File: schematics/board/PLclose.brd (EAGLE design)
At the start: 82 x 82 mm, 38 parts

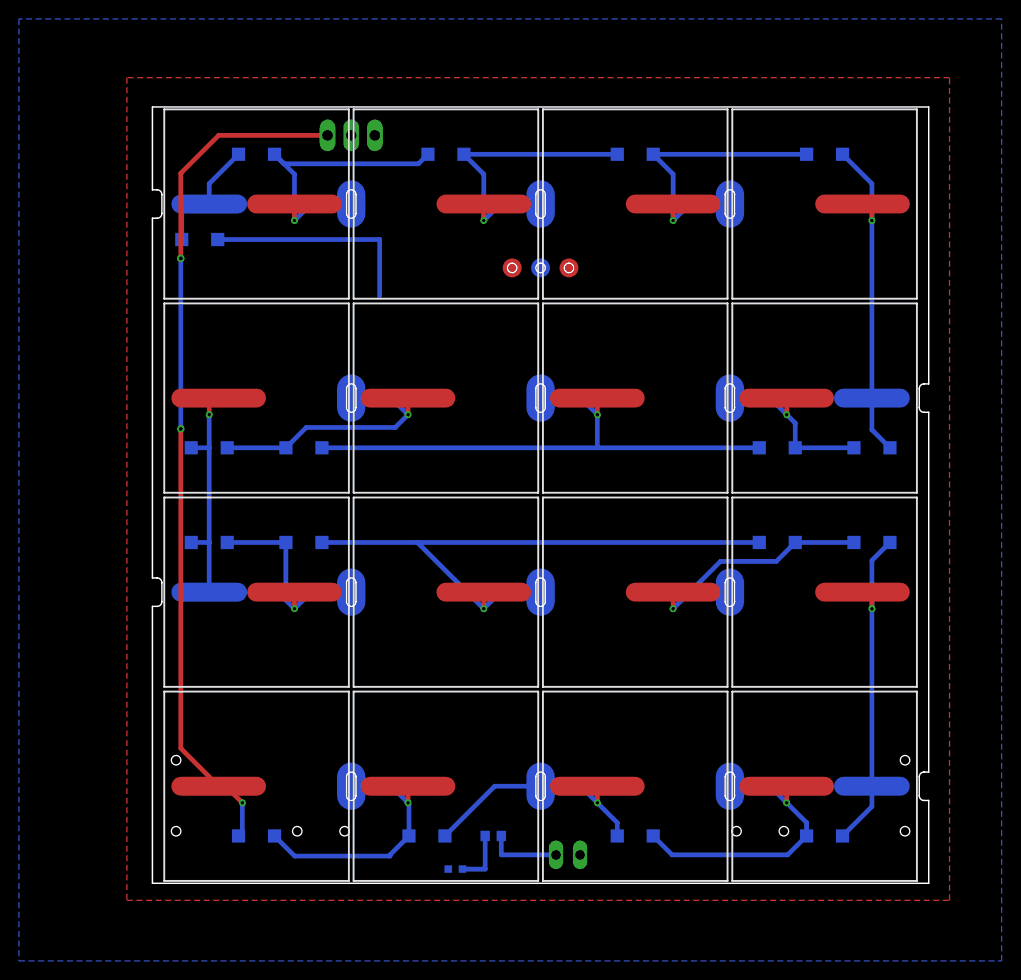
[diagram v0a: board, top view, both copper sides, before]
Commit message: Добавлена схема дозиметра, исправлены платы СБ
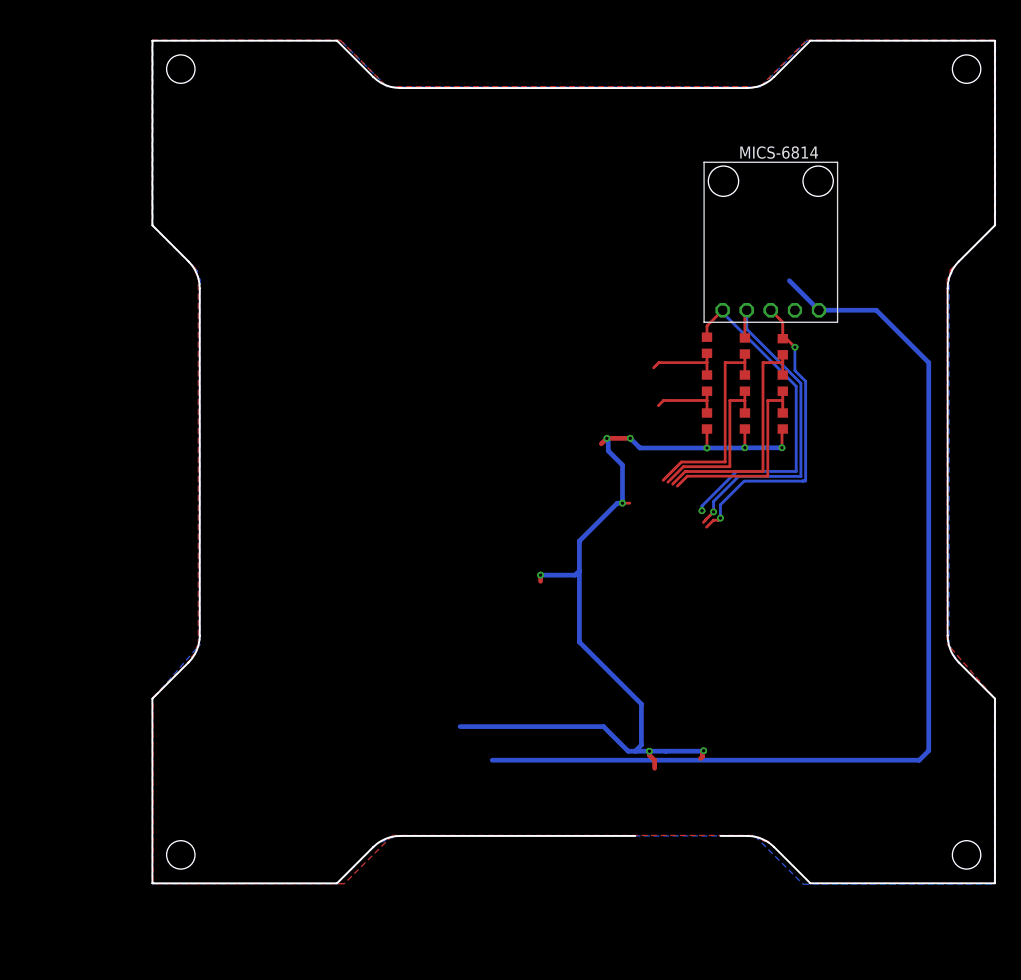
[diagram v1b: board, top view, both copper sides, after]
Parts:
- removed D1, D10, D11, D12, D13, D14, D15, D16, D17, D2, D3, D4, D5, D6, D7, D8, D9: MBR0520LT, diode:SOD123
- removed JP1: (no value), pinhead:1X02
- removed PWR: (no value), led:CHIPLED_0603
- removed R1_2K7: 2k7, rcl:R0603
- removed S1: (no value), CanCubeSat:255SB
- removed SOL1, SOL10, SOL11, SOL13, SOL14, SOL15, SOL2, SOL3, SOL5, SOL6, SOL7, SOL9: SOLAR_0, CanCubeSat:SOLAR_0
- removed SOL12, SOL16, SOL4, SOL8: SOLAR_1, CanCubeSat:SOLAR_1
- removed U$6: GRAFITGRAFIT3_1, CanCubeSat:GRAFIT3_1
- added MICS-6814: MICS-6814, CanCubeSat:MICS-6814
- added R1, R2, R3, R4, R5, R6, R7, R8, R9: 10k, resistor:R0603
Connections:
- removed net BUS+: JP1.2, R1_2K7.1, S1.2
- removed net BUS-: D1.C, JP1.1, PWR.C
- removed net N$1: D16.A, D17.C, SOL1.OUT, SOL2.IN
- removed net N$10: D10.A, D11.C, SOL7.OUT, SOL8.IN
- removed net N$11: D10.C, D9.A, SOL8.OUT, SOL9.IN
- removed net N$12: D8.A, D9.C, SOL10.IN, SOL9.OUT
- removed net N$13: D7.A, D8.C, SOL10.OUT, SOL11.IN
- removed net N$14: D6.A, D7.C, SOL11.OUT, SOL12.IN
- removed net N$15: D5.A, D6.C, SOL12.OUT, SOL13.IN
- removed net N$16: D4.A, D5.C, SOL13.OUT, SOL14.IN
- removed net N$17: D3.A, D4.C, SOL14.OUT, SOL15.IN
- removed net N$18: D2.A, D3.C, SOL15.OUT, SOL16.IN
- removed net N$24: D13.A, D14.C, SOL4.OUT, SOL5.IN
- removed net N$3: D15.A, D16.C, SOL2.OUT, SOL3.IN
- removed net N$4: D1.A, D2.C, SOL16.OUT
- removed net N$5: PWR.A, R1_2K7.2
- removed net N$6: D14.A, D15.C, SOL3.OUT, SOL4.IN
- removed net N$7: D17.A, S1.3, SOL1.IN
- removed net N$8: D12.A, D13.C, SOL5.OUT, SOL6.IN
- removed net N$9: D11.A, D12.C, SOL6.OUT, SOL7.IN
- new net 3V3: R7.2, R8.2, R9.2
- new net 5V: MICS-6814.P$1
- new net CO: MICS-6814.P$5, R3.1
- new net CTRL-CO-1: R3.2, R6.1
- new net CTRL-CO-2: R6.2, R7.1
- new net CTRL-NH3-1: R2.2, R5.1
- new net CTRL-NH3-2: R5.2, R8.1
- new net CTRL-NO2-1: R1.2, R4.1
- new net CTRL-NO2-2: R4.2, R9.1
- new net NH3: MICS-6814.P$4, R2.1
- new net NO2: MICS-6814.P$3, R1.1
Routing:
- net 5V: track 0.00 -> 105.8 mm
- net 3V3: track 0.00 -> 100.2 mm, vias 0 -> 9
- net N$7: track 90.6 -> 0.00 mm, vias 3 -> 0
- net N$9: track 64.6 -> 0.00 mm, vias 1 -> 0
- net N$13: track 58.2 -> 0.00 mm, vias 1 -> 0
- net NH3: track 0.00 -> 35.9 mm, vias 0 -> 1
- net CO: track 0.00 -> 35.9 mm, vias 0 -> 1
- net N$24: track 35.8 -> 0.00 mm, vias 1 -> 0
- net N$15: track 35.8 -> 0.00 mm, vias 1 -> 0
- net N$18: track 33.4 -> 0.00 mm, vias 1 -> 0
- net NO2: track 0.00 -> 33.1 mm, vias 0 -> 2
- net N$17: track 32.5 -> 0.00 mm, vias 1 -> 0
- net N$16: track 32.5 -> 0.00 mm, vias 1 -> 0
- net N$6: track 30.7 -> 0.00 mm, vias 1 -> 0
- net N$12: track 29.0 -> 0.00 mm, vias 1 -> 0
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- added copper zone on layer 1, net GND
- added copper zone on layer 16, net GND
- removed copper zone on layer 1, net BUS+
- removed copper zone on layer 16, net BUS-
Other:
- board size 82 x 82 mm -> 89 x 89 mm
- board text removed: "BUS+"
- board text removed: "BUS-"
- board text removed: "OFF"
- board text removed: "ON"
